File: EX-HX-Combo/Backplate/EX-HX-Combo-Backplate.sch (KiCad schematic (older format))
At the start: 1 part

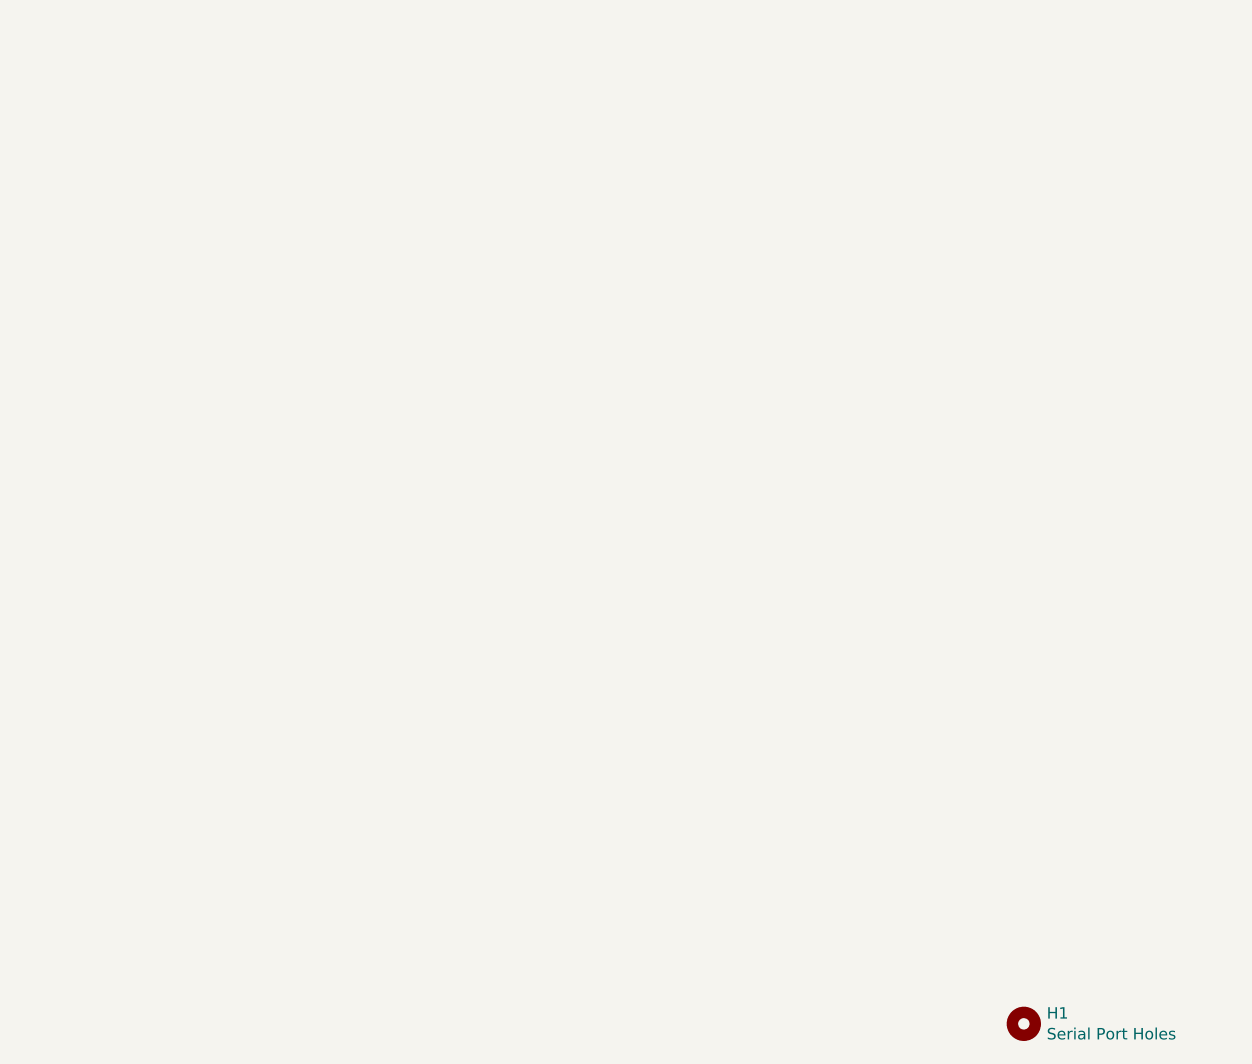
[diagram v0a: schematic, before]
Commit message: Alternative EX-HX-Combo-Backpate designed for Aluminium manufacture.
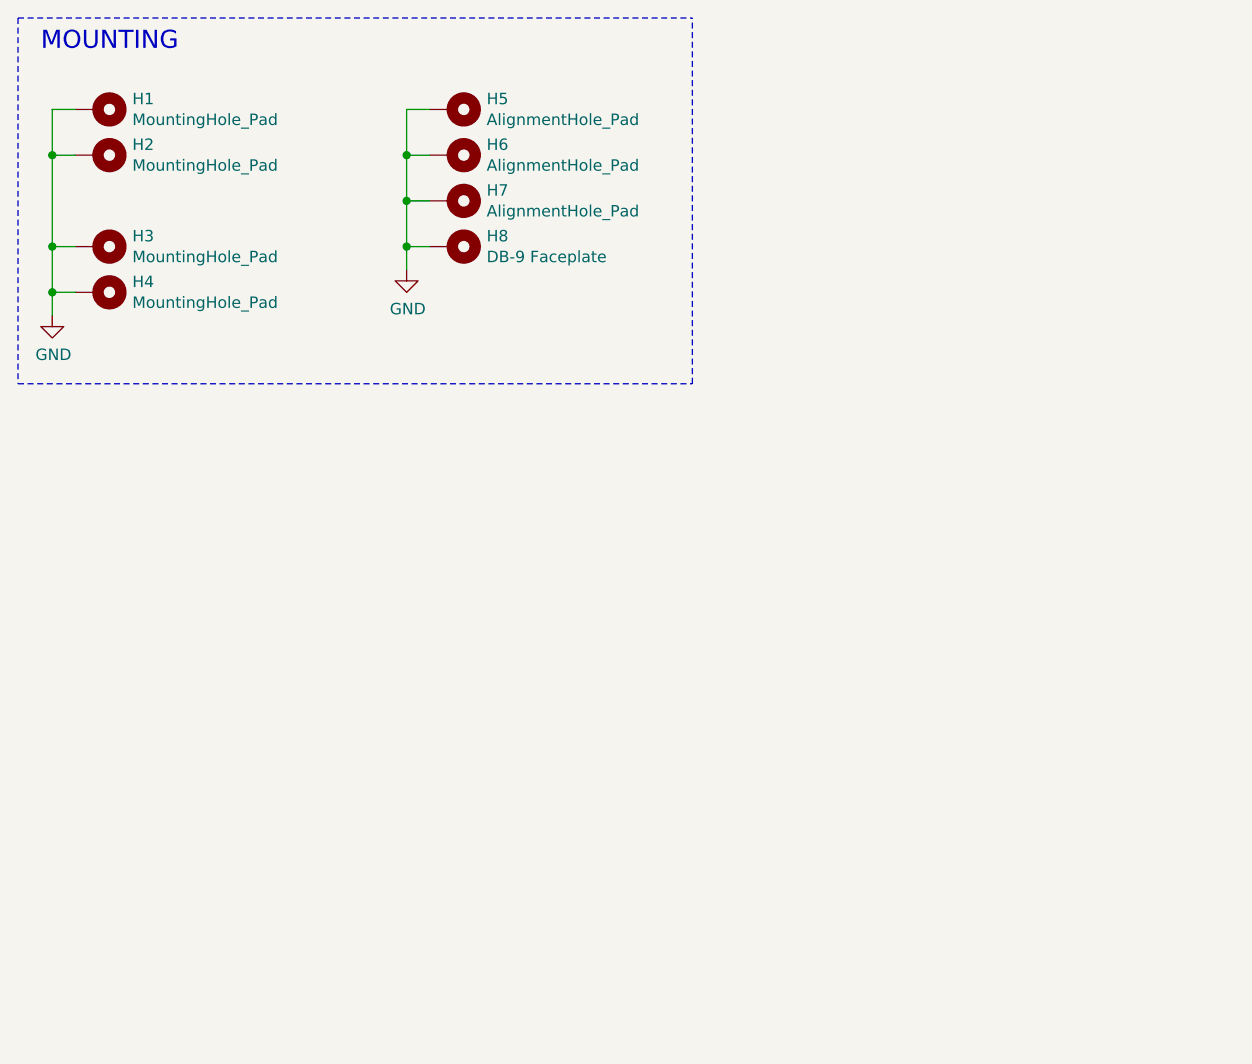
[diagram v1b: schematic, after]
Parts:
- removed H1: Serial Port Holes, 00Custom:DB9_Face_NPTH, symbol Mechanical:MountingHole
- added H1, H2, H3, H4: MountingHole_Pad, MountingHole:MountingHole_3.5mm_Pad, symbol Mechanical:MountingHole_Pad
- added H5, H6, H7: AlignmentHole_Pad, 00Custom:AlignmentHole, symbol Mechanical:MountingHole_Pad
- added H8: DB-9 Faceplate, 00Custom:DB9_Face, symbol Mechanical:MountingHole_Pad
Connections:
- new net GND: H1.1, H2.1, H3.1, H4.1, H5.1, H6.1, H7.1, H8.1
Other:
- note added: "MOUNTING"
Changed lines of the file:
@@
 $EndDescr
 $Comp
-L Mechanical:MountingHole H1
-U 1 1 611CEF27
-P 5000 5000
-F 0 "H1" H 5100 5046 50  0000 L CNN
-F 1 "Serial Port Holes" H 5100 4955 50  0000 L CNN
-F 2 "00Custom:DB9_Face_NPTH" H 5000 5000 50  0001 C CNN
-F 3 "~" H 5000 5000 50  0001 C CNN
-	1    5000 5000
+L Mechanical:MountingHole_Pad H1
+U 1 1 60D6AC46
+P 950 1000
+F 0 "H1" V 904 1150 50  0000 L CNN
+F 1 "MountingHole_Pad" V 995 1150 50  0000 L CNN
+F 2 "MountingHole:MountingHole_3.5mm_Pad" H 950 1000 50  0001 C CNN
+F 3 "~" H 950 1000 50  0001 C CNN
+	1    950  1000
+	0    1    1    0
+$EndComp
+$Comp
+L Mechanical:MountingHole_Pad H2
+U 1 1 60D6B05B
+P 950 1200
+F 0 "H2" V 904 1350 50  0000 L CNN
+F 1 "MountingHole_Pad" V 995 1350 50  0000 L CNN
+F 2 "MountingHole:MountingHole_3.5mm_Pad" H 950 1200 50  0001 C CNN
+F 3 "~" H 950 1200 50  0001 C CNN
+	1    950  1200
+	0    1    1    0
+$EndComp
+$Comp
+L Mechanical:MountingHole_Pad H3
+U 1 1 60D6B4F1
+P 950 1600
+F 0 "H3" V 904 1750 50  0000 L CNN
+F 1 "MountingHole_Pad" V 995 1750 50  0000 L CNN
+F 2 "MountingHole:MountingHole_3.5mm_Pad" H 950 1600 50  0001 C CNN
+F 3 "~" H 950 1600 50  0001 C CNN
+	1    950  1600
+	0    1    1    0
+$EndComp
+Wire Wire Line
+	850  1600 750  1600
+Connection ~ 750  1600
+Wire Wire Line
+	750  1600 750  1800
+$Comp
+L Mechanical:MountingHole_Pad H4
+U 1 1 60D9AE58
+P 950 1800
+F 0 "H4" V 904 1950 50  0000 L CNN
+F 1 "MountingHole_Pad" V 995 1950 50  0000 L CNN
+F 2 "MountingHole:MountingHole_3.5mm_Pad" H 950 1800 50  0001 C CNN
+F 3 "~" H 950 1800 50  0001 C CNN
+	1    950  1800
+	0    1    1    0
+$EndComp
+Wire Wire Line
+	850  1800 750  1800
+Connection ~ 750  1800
+Wire Wire Line
+	750  1800 750  1900
+$Comp
+L power:GND #PWR0148
+U 1 1 60DA739E
+P 750 1900
+F 0 "#PWR0148" H 750 1650 50  0001 C CNN
+F 1 "GND" H 755 1727 50  0000 C CNN
+F 2 "" H 750 1900 50  0001 C CNN
+F 3 "" H 750 1900 50  0001 C CNN
+	1    750  1900
 	1    0    0    -1
 $EndComp
+Wire Wire Line
+	850  1200 750  1200
+Connection ~ 750  1200
+Wire Wire Line
+	850  1000 750  1000
+Wire Wire Line
+	750  1000 750  1200
+Wire Wire Line
+	750  1200 750  1600
+$Comp
+L Mechanical:MountingHole_Pad H5
+U 1 1 61187FCA
+P 2500 1000
+F 0 "H5" V 2454 1150 50  0000 L CNN
+F 1 "AlignmentHole_Pad" V 2545 1150 50  0000 L CNN
+F 2 "00Custom:AlignmentHole" H 2500 1000 50  0001 C CNN
+F 3 "~" H 2500 1000 50  0001 C CNN
+	1    2500 1000
+	0    1    1    0
+$EndComp
+$Comp
+L Mechanical:MountingHole_Pad H6
+U 1 1 611A4105
+P 2500 1200
+F 0 "H6" V 2454 1350 50  0000 L CNN
+F 1 "AlignmentHole_Pad" V 2545 1350 50  0000 L CNN
+F 2 "00Custom:AlignmentHole" H 2500 1200 50  0001 C CNN
+F 3 "~" H 2500 1200 50  0001 C CNN
+	1    2500 1200
+	0    1    1    0
+$EndComp
+$Comp
+L Mechanical:MountingHole_Pad H7
+U 1 1 611C6C9E
+P 2500 1400
+F 0 "H7" V 2454 1550 50  0000 L CNN
+F 1 "AlignmentHole_Pad" V 2545 1550 50  0000 L CNN
+F 2 "00Custom:AlignmentHole" H 2500 1400 50  0001 C CNN
+F 3 "~" H 2500 1400 50  0001 C CNN
+	1    2500 1400
+	0    1    1    0
+$EndComp
+Wire Wire Line
+	2400 1000 2300 1000
+Wire Wire Line
+	2300 1000 2300 1200
+Wire Wire Line
+	2400 1200 2300 1200
+Connection ~ 2300 1200
+Wire Wire Line
+	2300 1200 2300 1400
+Wire Wire Line
+	2400 1400 2300 1400
+Text Notes 700  750  0    79   ~ 0
+MOUNTING
+Wire Notes Line
+	600  600  600  2200
+Wire Notes Line
+	600  600  3550 600
+Wire Notes Line
+	600  2200 3550 2200
+Wire Notes Line
+	3550 2200 3550 600
+Connection ~ 2300 1400
+Wire Wire Line
+	2300 1600 2300 1700
+Connection ~ 2300 1600
+Wire Wire Line
+	2400 1600 2300 1600
+Wire Wire Line
+	2300 1400 2300 1600
+$Comp
+L Mechanical:MountingHole_Pad H8
+U 1 1 611975A0
+P 2500 1600
+F 0 "H8" V 2454 1750 50  0000 L CNN
+F 1 "DB-9 Faceplate" V 2545 1750 50  0000 L CNN
+F 2 "00Custom:DB9_Face" H 2500 1600 50  0001 C CNN
+F 3 "~" H 2500 1600 50  0001 C CNN
+	1    2500 1600
+	0    1    1    0
+$EndComp
+$Comp
+L power:GND #PWR0179
+U 1 1 6120C5C6
+P 2300 1700
+F 0 "#PWR0179" H 2300 1450 50  0001 C CNN
+F 1 "GND" H 2305 1527 50  0000 C CNN
+F 2 "" H 2300 1700 50  0001 C CNN
+F 3 "" H 2300 1700 50  0001 C CNN
+	1    2300 1700
+	1    0    0    -1
+$EndComp

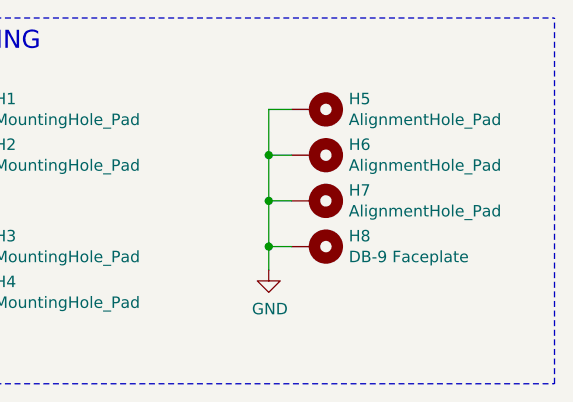
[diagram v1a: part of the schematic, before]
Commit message: EX-HX-Combo: Relocate back plate alignment tabs to very ends of boards. Also make them 1mm narrower. Remove middle alighment tab.
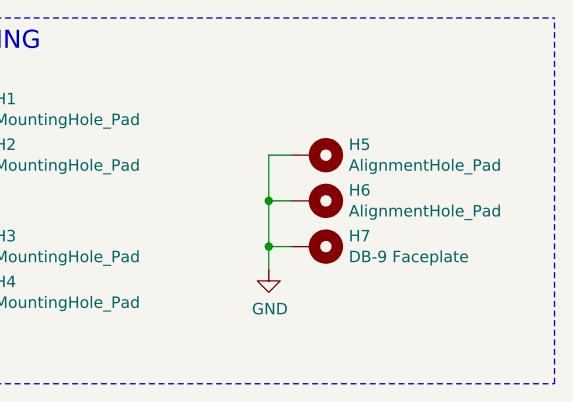
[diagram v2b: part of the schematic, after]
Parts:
- removed H6: AlignmentHole_Pad, 00Custom:AlignmentHole, symbol Mechanical:MountingHole_Pad
- renumbered H7 to H6, H8 to H7
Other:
- moved on the sheet: H5
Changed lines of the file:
@@
 L Mechanical:MountingHole_Pad H5
 U 1 1 61187FCA
-P 2500 1000
-F 0 "H5" V 2454 1150 50  0000 L CNN
-F 1 "AlignmentHole_Pad" V 2545 1150 50  0000 L CNN
-F 2 "00Custom:AlignmentHole" H 2500 1000 50  0001 C CNN
-F 3 "~" H 2500 1000 50  0001 C CNN
-	1    2500 1000
-	0    1    1    0
-$EndComp
-$Comp
-L Mechanical:MountingHole_Pad H6
-U 1 1 611A4105
 P 2500 1200
-F 0 "H6" V 2454 1350 50  0000 L CNN
+F 0 "H5" V 2454 1350 50  0000 L CNN
 F 1 "AlignmentHole_Pad" V 2545 1350 50  0000 L CNN
 F 2 "00Custom:AlignmentHole" H 2500 1200 50  0001 C CNN
@@
 $EndComp
 $Comp
-L Mechanical:MountingHole_Pad H7
+L Mechanical:MountingHole_Pad H6
 U 1 1 611C6C9E
 P 2500 1400
-F 0 "H7" V 2454 1550 50  0000 L CNN
+F 0 "H6" V 2454 1550 50  0000 L CNN
 F 1 "AlignmentHole_Pad" V 2545 1550 50  0000 L CNN
 F 2 "00Custom:AlignmentHole" H 2500 1400 50  0001 C CNN
@@
 $EndComp
 Wire Wire Line
-	2400 1000 2300 1000
-Wire Wire Line
-	2300 1000 2300 1200
-Wire Wire Line
 	2400 1200 2300 1200
-Connection ~ 2300 1200
 Wire Wire Line
 	2300 1200 2300 1400
@@
 	2300 1400 2300 1600
 $Comp
-L Mechanical:MountingHole_Pad H8
+L Mechanical:MountingHole_Pad H7
 U 1 1 611975A0
 P 2500 1600
-F 0 "H8" V 2454 1750 50  0000 L CNN
+F 0 "H7" V 2454 1750 50  0000 L CNN
 F 1 "DB-9 Faceplate" V 2545 1750 50  0000 L CNN
 F 2 "00Custom:DB9_Face" H 2500 1600 50  0001 C CNN
